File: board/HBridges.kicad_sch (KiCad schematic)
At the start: 36 parts, among them Q1 NMOS, Q2 NMOS, Q3 NMOS, Q4 NMOS, Q5 NMOS, Q6 NMOS

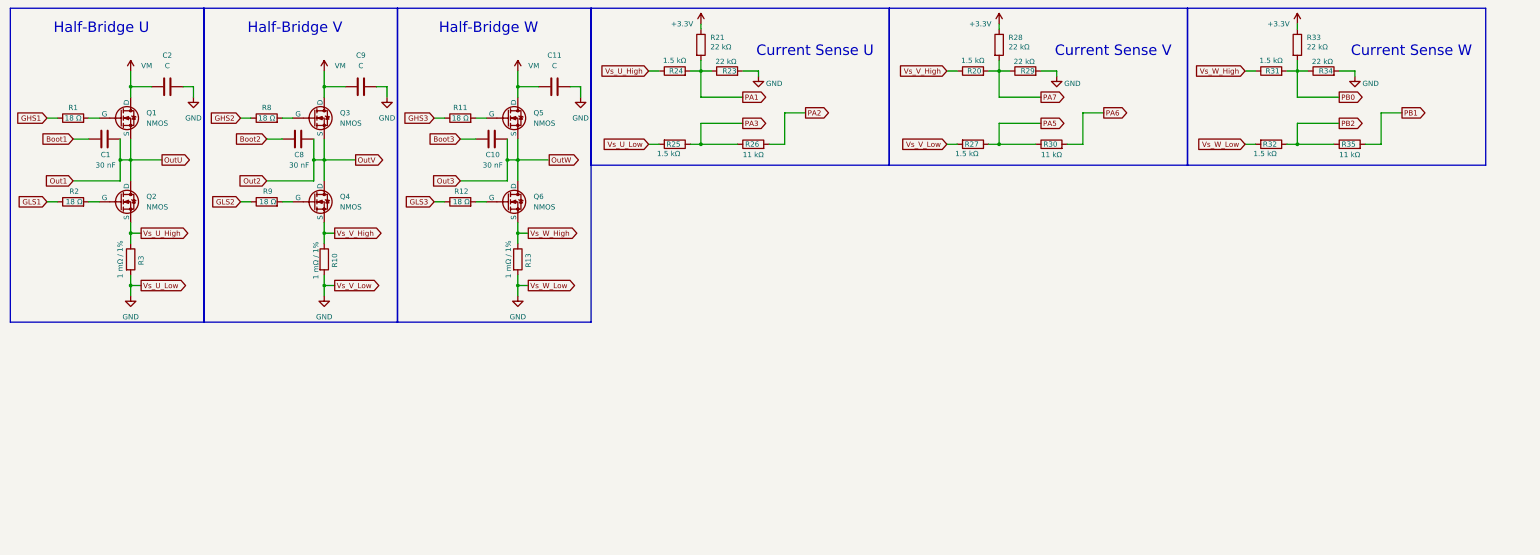
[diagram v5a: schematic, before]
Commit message: Fixed many issues brought up in the schematic review.
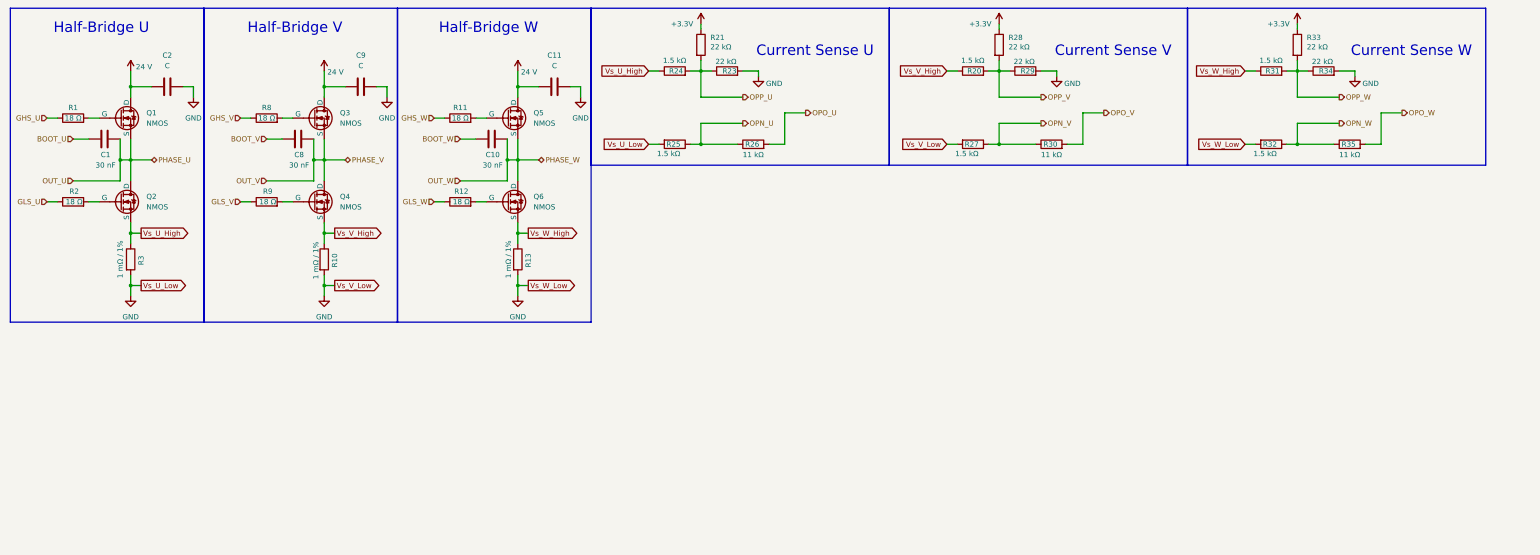
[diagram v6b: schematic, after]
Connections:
- net Boot1 renamed BOOT_U
- net Boot2 renamed BOOT_V
- net Boot3 renamed BOOT_W
- net GHS1 renamed GHS_U
- net GHS2 renamed GHS_V
- net GHS3 renamed GHS_W
- net GLS1 renamed GLS_U
- net GLS2 renamed GLS_V
- net GLS3 renamed GLS_W
- net Out1 renamed OUT_U
- net Out2 renamed OUT_V
- net Out3 renamed OUT_W
- net PA1 renamed OPP_U
- net PA2 renamed OPO_U
- net PA3 renamed OPN_U
- net PA5 renamed OPN_V
- net PA6 renamed OPO_V
- net PA7 renamed OPP_V
- net PB0 renamed OPP_W
- net PB1 renamed OPO_W
- net PB2 renamed OPN_W
- net VM renamed 24 V

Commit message: Fixed everything mentioned in schematic review, should be ready for second review/layout.
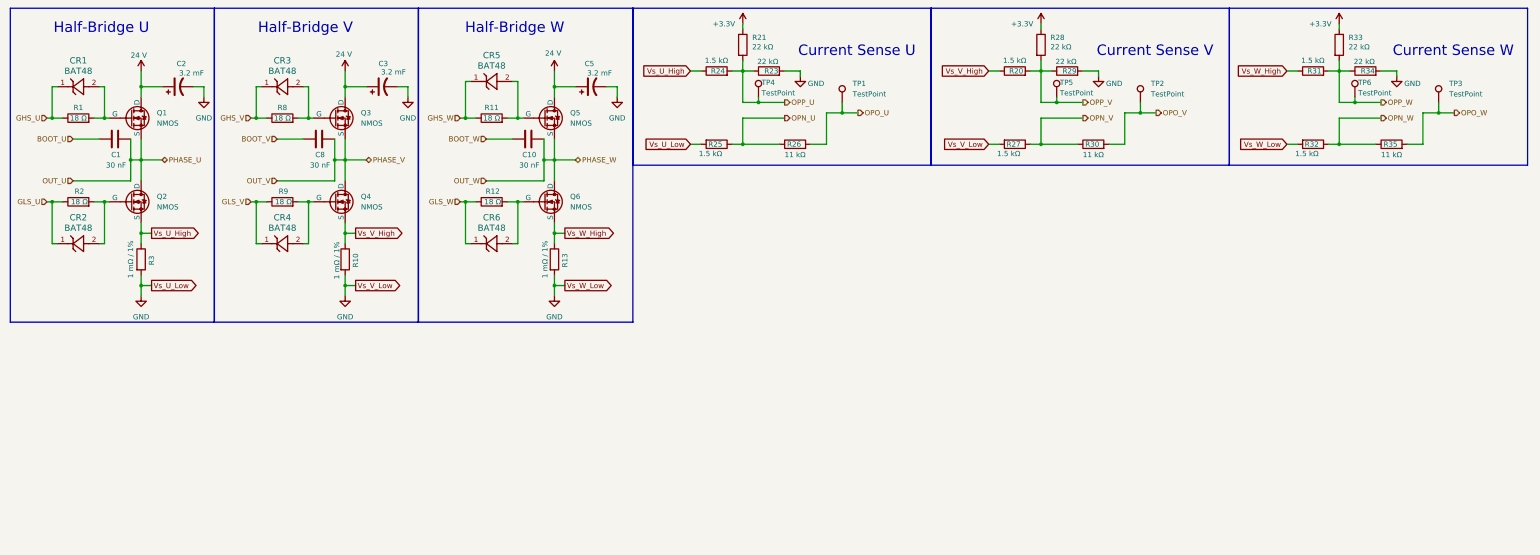
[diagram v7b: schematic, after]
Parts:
- removed C11, C2, C9: C, symbol Device:C
- added C2, C3, C5: 3.2 mF, symbol Device:C_Polarized_US
- added CR1, CR2, CR3, CR4, CR5, CR6: BAT48, DO-35_STM, symbol BAT48:BAT48
- added TP1, TP2, TP3, TP4, TP5, TP6: TestPoint, symbol Connector:TestPoint
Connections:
- net 24 V: now also C2.1, C3.1, C5.1
- net GHS_U: now also CR1.1
- net GHS_V: now also CR3.1
- net GHS_W: now also CR5.1
- net GLS_U: now also CR2.1
- net GLS_V: now also CR4.1
- net GLS_W: now also CR6.1
- net GND: now also C2.2, C3.2, C5.2
- net OPO_U: now also TP1.1
- net OPO_V: now also TP2.1
- net OPO_W: now also TP3.1
- net OPP_U: now also TP4.1
- net OPP_V: now also TP5.1
- net OPP_W: now also TP6.1
- net at Q5.2 (G), R11.2: now also CR5.2
- net at Q6.2 (G), R12.2: now also CR6.2
- net at Q4.2 (G), R9.2: now also CR4.2
- net at Q2.2 (G), R2.2: now also CR2.2
- net at Q1.2 (G), R1.2: now also CR1.2
- net at Q3.2 (G), R8.2: now also CR3.2
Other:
- moved on the sheet: C1, C10, C8, Q1, Q2, Q3, Q4, Q5, Q6, R1, R10, R11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

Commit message: Updated footprints for schematic
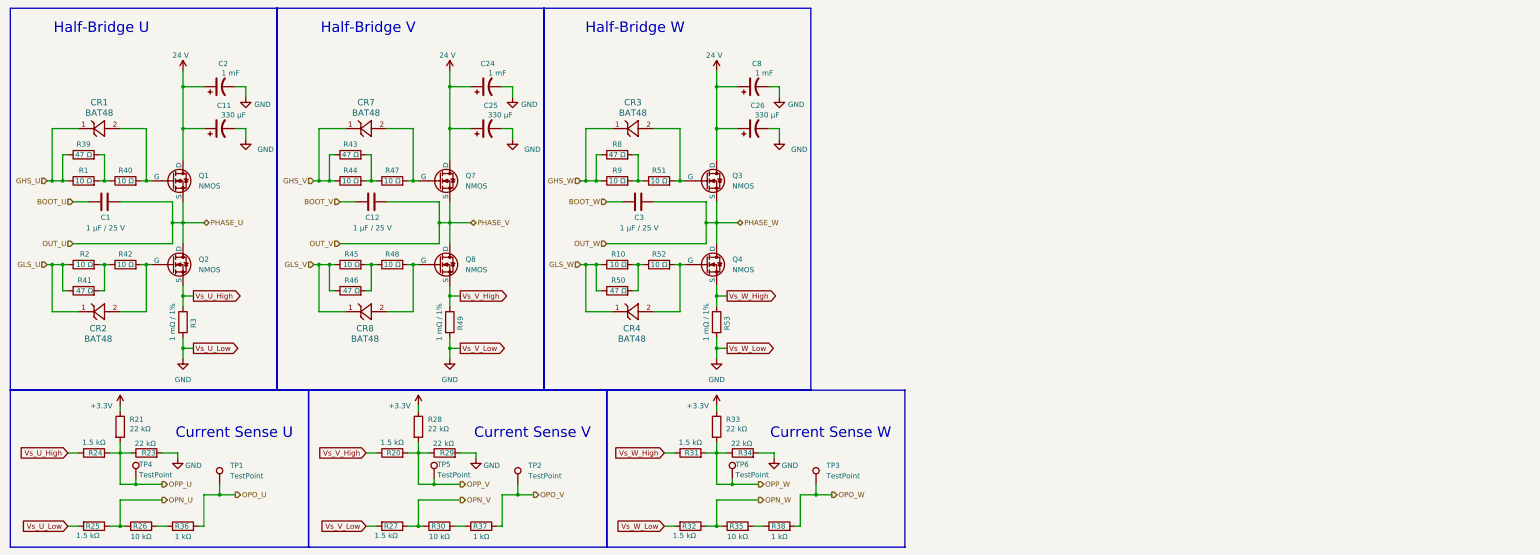
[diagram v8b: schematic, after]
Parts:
- removed C10, C8: 30 nF, symbol Device:C
- removed C3, C5: 3.2 mF, symbol Device:C_Polarized_US
- removed CR5, CR6: BAT48, DO-35_STM, symbol BAT48:BAT48
- removed Q5, Q6: NMOS, symbol Simulation_SPICE:NMOS
- removed R11, R12: 18 Ω, symbol Device:R
- removed R13: 1 mΩ / 1%, symbol Device:R
- added C11, C25, C26: 330 μF, BoCoFootprintLibrary:CAP_PAN_EEE_H13_PAN, symbol Device:C_Polarized_US
- added C12, C3: 1 µF / 25 V, Capacitor_SMD:C_0603_1608Metric_Pad1.08x0.95mm_HandSolder, symbol Device:C
- added C24, C8: 1 mF, BoCoFootprintLibrary:U1-Z_NCH, symbol Device:C_Polarized_US
- added CR7, CR8: BAT48, BoCoFootprintLibrary:DO-35_STM, symbol BAT48:BAT48
- added Q7, Q8: NMOS, BoCoFootprintLibrary:PG-TDSON-8_INF, symbol Simulation_SPICE:NMOS
- added R36, R37, R38: 1 kΩ, Resistor_SMD:R_0603_1608Metric_Pad0.98x0.95mm_HandSolder, symbol Device:R
- added R39, R41, R43, R46, R50: 47 Ω, Resistor_SMD:R_0603_1608Metric_Pad0.98x0.95mm_HandSolder, symbol Device:R
- added R40, R42, R44, R45, R47, R48, R51, R52: 10 Ω, Resistor_SMD:R_0603_1608Metric_Pad0.98x0.95mm_HandSolder, symbol Device:R
- added R49, R53: 1 mΩ / 1%, Resistor_SMD:R_0603_1608Metric_Pad0.98x0.95mm_HandSolder, symbol Device:R
- C1: value 30 nF -> 1 µF / 25 V; footprint (none) -> Capacitor_SMD:C_0603_1608Metric_Pad1.08x0.95mm_HandSolder
- C2: value 3.2 mF -> 1 mF; footprint (none) -> BoCoFootprintLibrary:U1-Z_NCH
- CR1, CR2, CR3, CR4: footprint DO-35_STM -> BoCoFootprintLibrary:DO-35_STM
- Q1, Q2, Q3, Q4: footprint (none) -> BoCoFootprintLibrary:PG-TDSON-8_INF
- R1, R2, R9: value 18 Ω -> 10 Ω; footprint (none) -> Resistor_SMD:R_0603_1608Metric_Pad0.98x0.95mm_HandSolder
- R10: value 1 mΩ / 1% -> 10 Ω; footprint (none) -> Resistor_SMD:R_0603_1608Metric_Pad0.98x0.95mm_HandSolder
- R20, R21, R23, R24, R25, R27, R28, R29, R3, R31, R32, R33, R34: footprint (none) -> Resistor_SMD:R_0603_1608Metric_Pad0.98x0.95mm_HandSolder
- R26, R30, R35: value 11 kΩ -> 10 kΩ; footprint (none) -> Resistor_SMD:R_0603_1608Metric_Pad0.98x0.95mm_HandSolder
- R8: value 18 Ω -> 47 Ω; footprint (none) -> Resistor_SMD:R_0603_1608Metric_Pad0.98x0.95mm_HandSolder
- TP1, TP2, TP3, TP4, TP5, TP6: footprint (none) -> TestPoint:TestPoint_Pad_D4.0mm
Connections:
- net 24 V: now also C11.1, C24.1, C25.1, C26.1, C8.1, Q7.1 (D)
- net BOOT_V: now also C12.1
- net BOOT_W: now also C3.1
- net GHS_U: now also R39.1
- net GHS_V: now also CR7.1, R43.1, R44.1; no longer CR3.1, R8.1
- net GHS_W: now also CR3.1, R8.1, R9.1
- net GLS_U: now also R41.1
- net GLS_V: now also CR8.1, R45.1, R46.1; no longer CR4.1, R9.1
- net GLS_W: now also CR4.1, R10.1, R50.1
- net GND: now also C11.2, C24.2, C25.2, C26.2, C8.2, R49.2, R53.2; no longer R10.2
- net OPO_U: now also R36.2; no longer R26.2
- net OPO_V: now also R37.2; no longer R30.2
- net OPO_W: now also R38.2; no longer R35.2
- net OUT_V: now also C12.2, Q7.3 (S), Q8.1 (D); no longer Q3.3 (S), Q4.1 (D)
- net OUT_W: now also Q3.3 (S), Q4.1 (D), C3.2
- net Vs_V_High: now also Q8.3 (S), R49.1; no longer Q4.3 (S), R10.1
- net Vs_W_High: now also Q4.3 (S), R53.1
- net at CR4.2, Q4.2 (G): now also R52.2; no longer R9.2
- net at CR2.2, Q2.2 (G): now also R42.2; no longer R2.2
- net at CR1.2, Q1.2 (G): now also R40.2; no longer R1.2
- net at CR3.2, Q3.2 (G): now also R51.2; no longer R8.2
- new net: R10.2, R50.2, R52.1
- new net: R30.2, R37.1
- new net: R2.2, R41.2, R42.1
- new net: R43.2, R44.2, R47.1
- new net: CR7.2, Q7.2 (G), R47.2
- new net: R35.2, R38.1
- new net: CR8.2, Q8.2 (G), R48.2
- new net: R1.2, R39.2, R40.1
- new net: R45.2, R46.2, R48.1
- new net: R26.2, R36.1
- new net: R51.1, R8.2, R9.2
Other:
- moved on the sheet: C1, C2, CR1, CR2, Q1, Q2, R1, R2, R20, R21, R23, R24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
